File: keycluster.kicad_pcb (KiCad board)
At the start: 2 copper layers, 45.1 x 52.6 mm, 62 parts, among them P2 CONN_5, P7 CONN_10, P8 CONN_7, U1 MKL03Z32VFK4, U2 IS31FL3737, U4 ESD

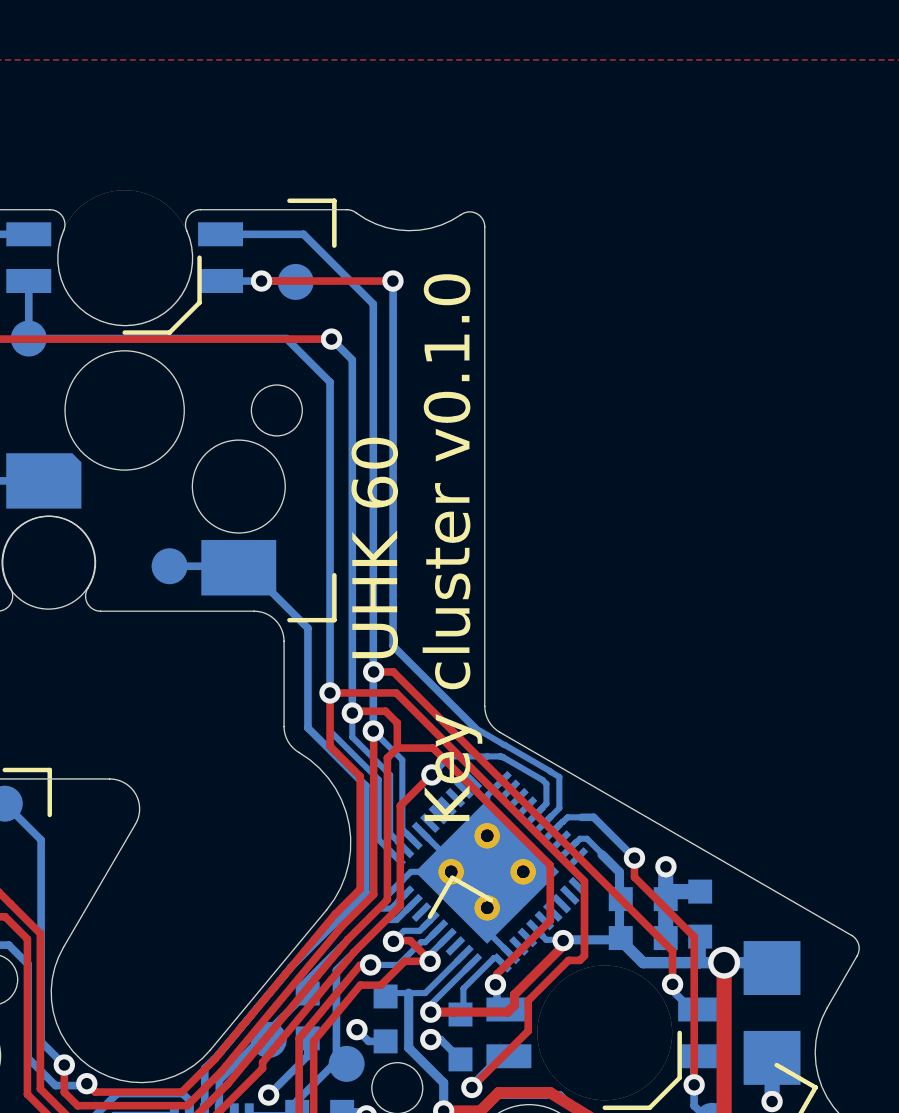
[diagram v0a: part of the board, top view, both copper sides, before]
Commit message: Modified varsion number on main board. 0.1.0 -> 1.0.0
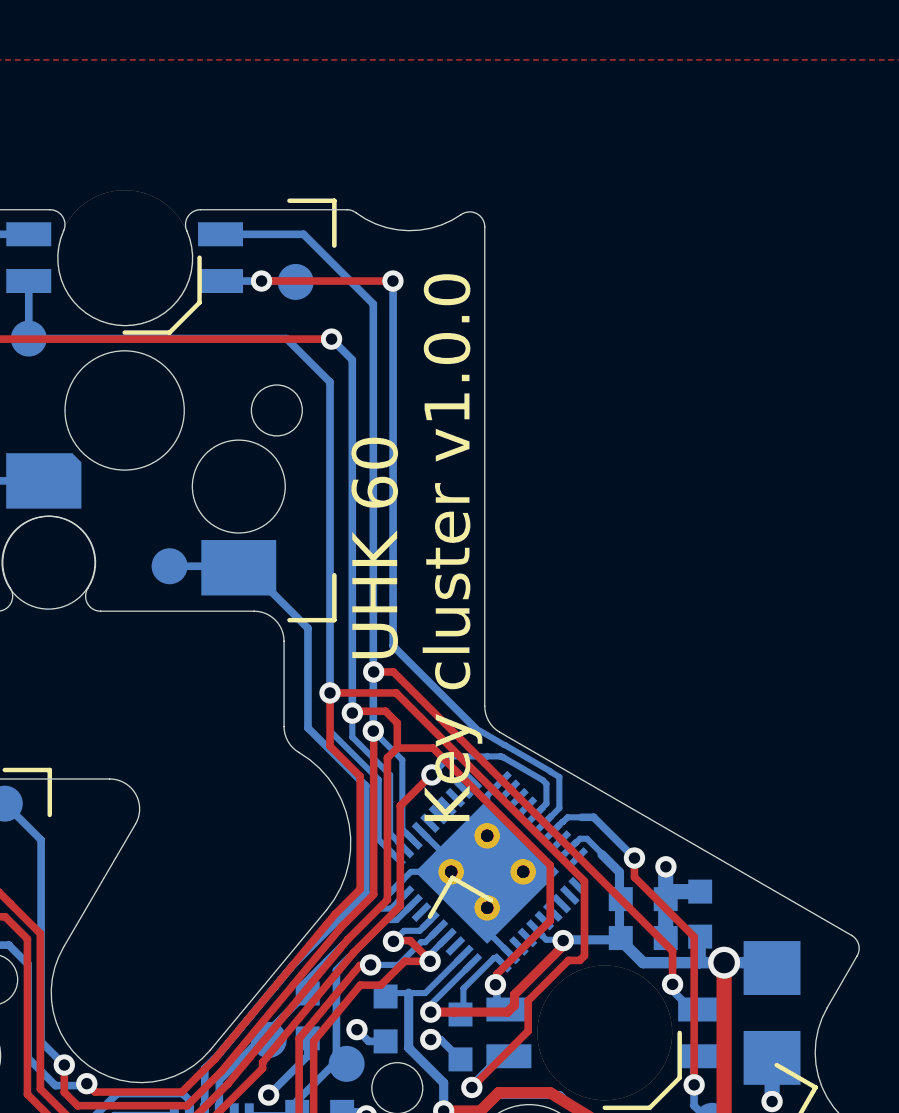
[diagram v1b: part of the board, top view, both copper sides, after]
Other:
- board text added: "UHK 60 Key cluster v1.0.0"
- board text removed: "UHK 60 Key cluster v0.1.0"
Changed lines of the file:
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@@
   (title_block
     (title "UHK 60 Key cluster main board")
-    (rev 0.1.0)
+    (rev 1.0.0)
     (company "Ultimate Gadget Laboratories Kft.")
   )
   (layers
-    (0 F.Cu signal hide)
+    (0 F.Cu signal)
     (31 B.Cu signal)
     (32 B.Adhes user)
@@
     (36 B.SilkS user)
     (37 F.SilkS user)
-    (38 B.Mask user hide)
-    (39 F.Mask user hide)
+    (38 B.Mask user)
+    (39 F.Mask user)
     (40 Dwgs.User user)
     (41 Cmts.User user)
@@
   )
   (setup
-    (last_trace_width 0.381)
+    (last_trace_width 0.2032)
     (user_trace_width 0.2032)
     (user_trace_width 0.254)
@@
     )
   )
-  (gr_text "UHK 60\nKey cluster v0.1.0" (at 152.309512 92.310302 90) (layer F.SilkS)
+  (gr_text "UHK 60\nKey cluster v1.0.0" (at 152.309512 92.310302 90) (layer F.SilkS)
     (effects (font (size 1.5 1.5) (thickness 0.3)))
   )

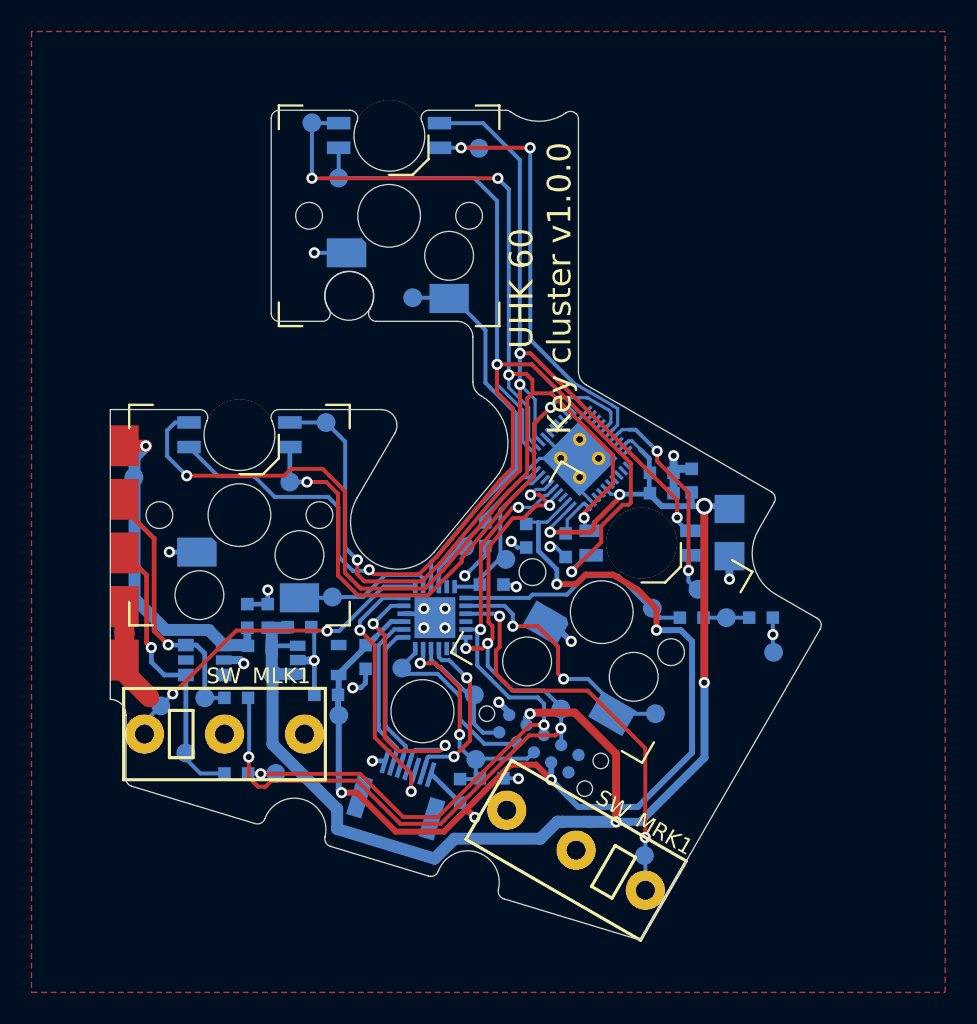
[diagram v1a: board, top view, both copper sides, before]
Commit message: Update key cluster contour.
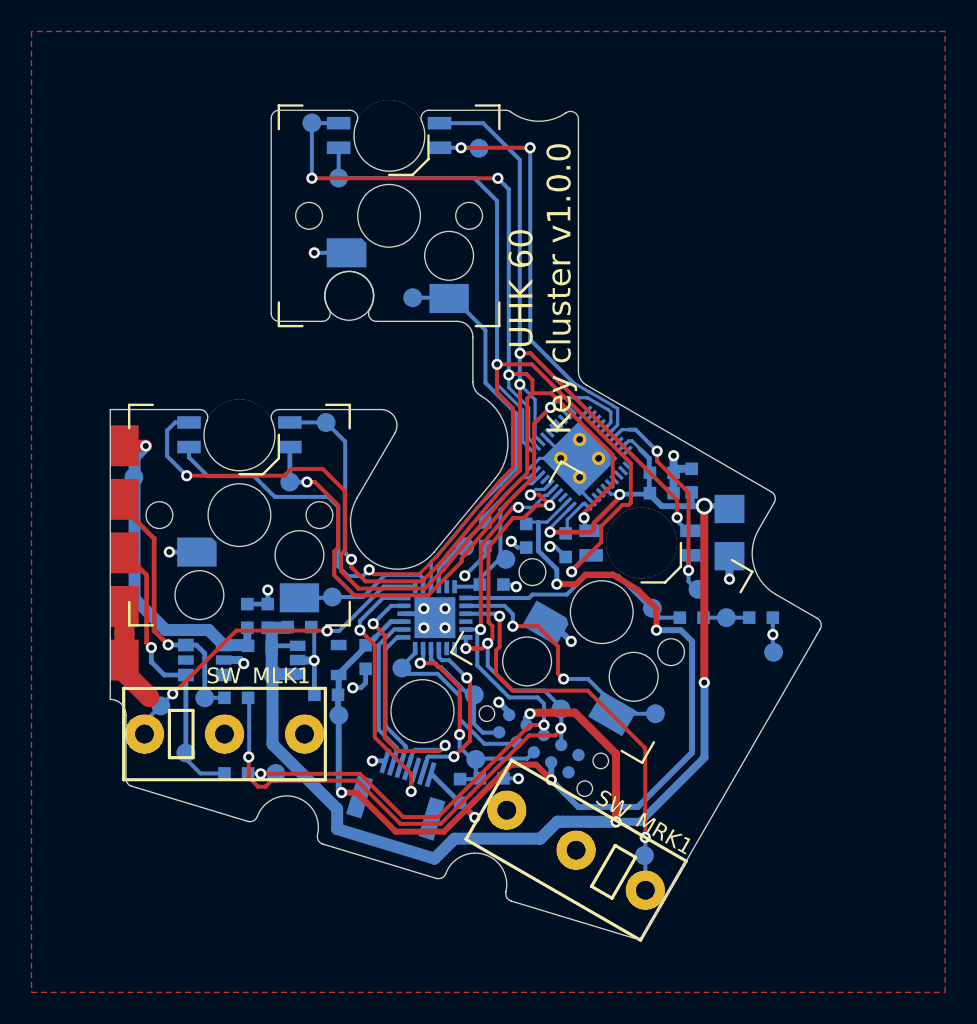
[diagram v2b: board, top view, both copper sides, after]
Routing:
- net /LED_SW1: track 86.8 -> 87.9 mm
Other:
- outline, holes or cut-outs redrawn
